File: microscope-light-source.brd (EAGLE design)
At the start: 35.6 x 50.8 mm, 17 parts, among them IC1 AVR-ATTINY13-DIP8, IC2 LM317, IC3 7805, J1 LED, J2 POT, J3 SINE, J4 SPARES, T1 2N7000

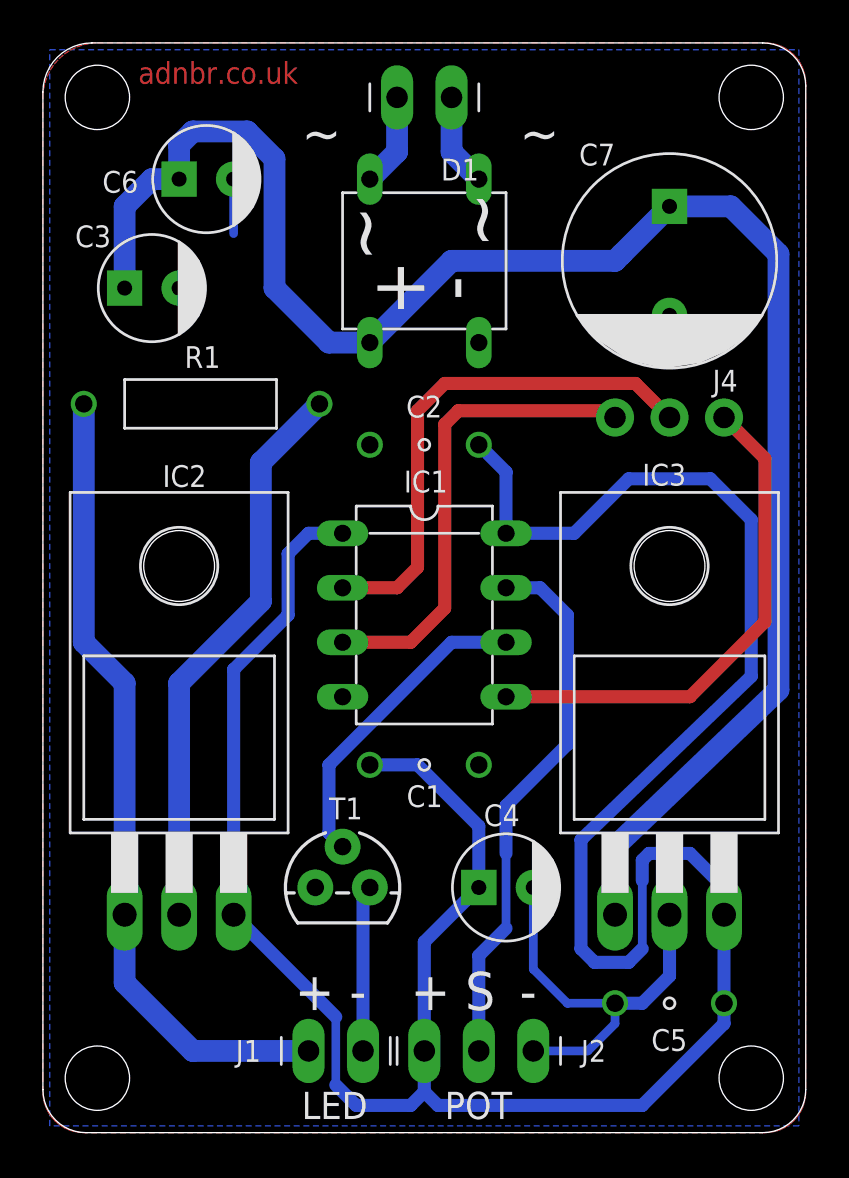
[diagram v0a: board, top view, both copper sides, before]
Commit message: C values, board re-jig
Values added for capacitors.
Voltage regulator rotated 180 deg to simplify trace routing.
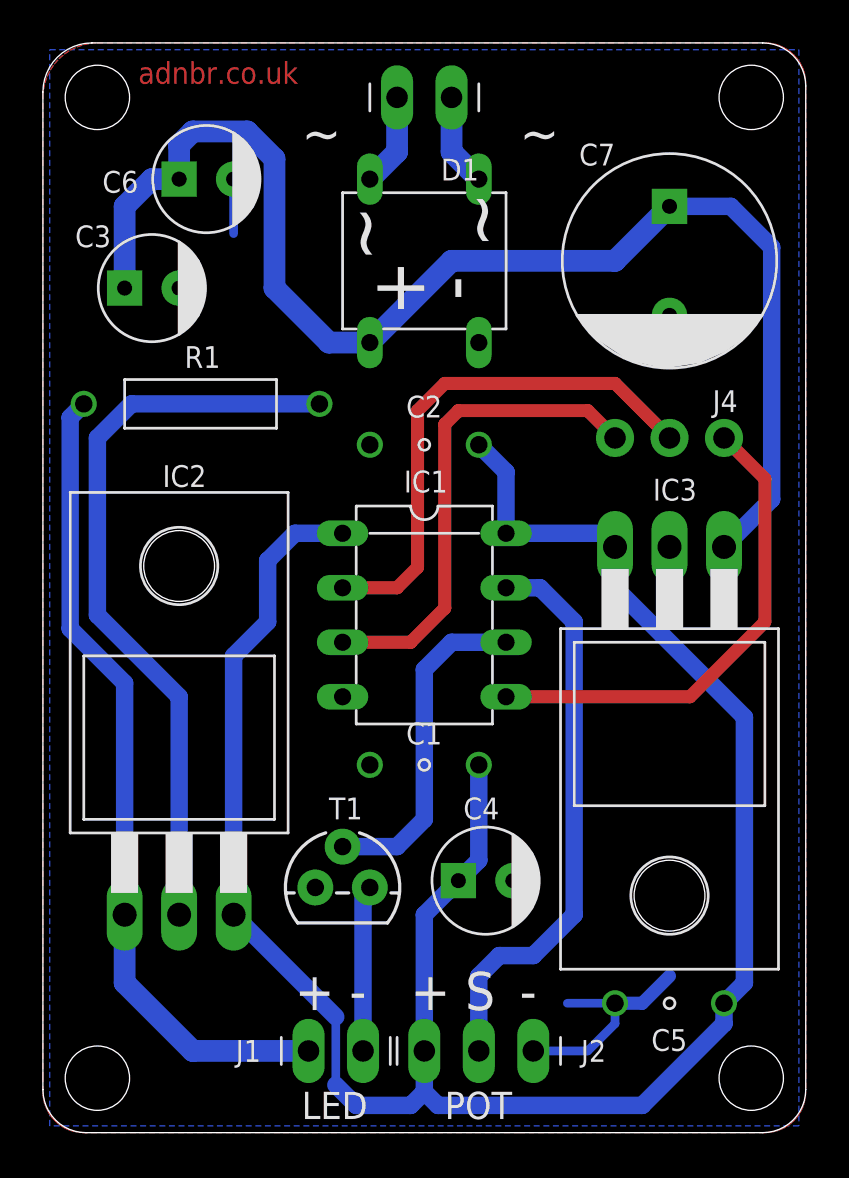
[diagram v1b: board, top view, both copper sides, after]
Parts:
- C3: value (none) -> 22uF
- C4, C6: value (none) -> 220uF
- C5: value (none) -> 10nF
- C7: value (none) -> 470uF
- IC3: value 7805 -> MCP1826S-5V
- moved C4 1.00 mm to (20.6, 11.7)
- moved J4 0.95 mm to (31.8, 32.4)
- moved IC3 0.64 mm to (29.2, 18.4), turned to 180 degrees
- turned C1 to 180 degrees
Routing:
- net +5V: track 130.8 -> 103.1 mm
- net N$7: track 81.9 -> 62.3 mm
- net GND: track 22.0 -> 13.1 mm
- net N$1: track 26.5 -> 34.8 mm
- net N$5: track 25.4 -> 26.6 mm
- net PWM: track 14.7 -> 15.7 mm
- net N$10: track 23.8 -> 22.9 mm
- net N$2: track 37.7 -> 38.2 mm
